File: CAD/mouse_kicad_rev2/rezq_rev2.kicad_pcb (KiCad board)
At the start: 2 copper layers, 92.8 x 89.3 mm, 99 parts, among them J2 SWD Header, M1 M1_Conn_Alt, M2 M2_Conn_Alt, Q0 TEFT4300, Q1 TEFT4300, Q10 Q_NMOS_GSD, Q11 Q_NMOS_GSD, Q12 Q_NMOS_GSD, Q2 TEFT4300, Q3 TEFT4300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

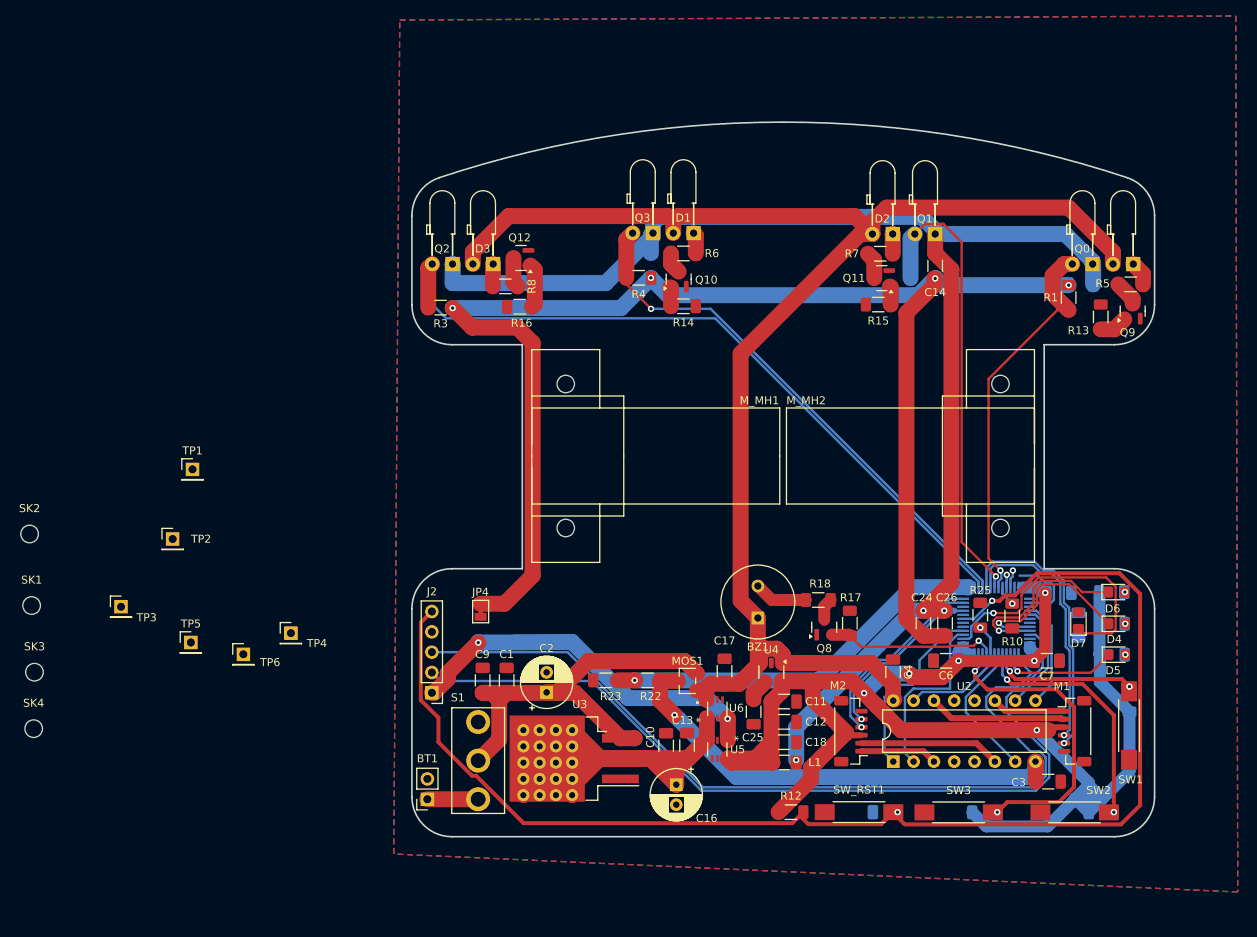
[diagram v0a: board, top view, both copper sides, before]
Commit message: Routed more of the schematic, connected all ground planes
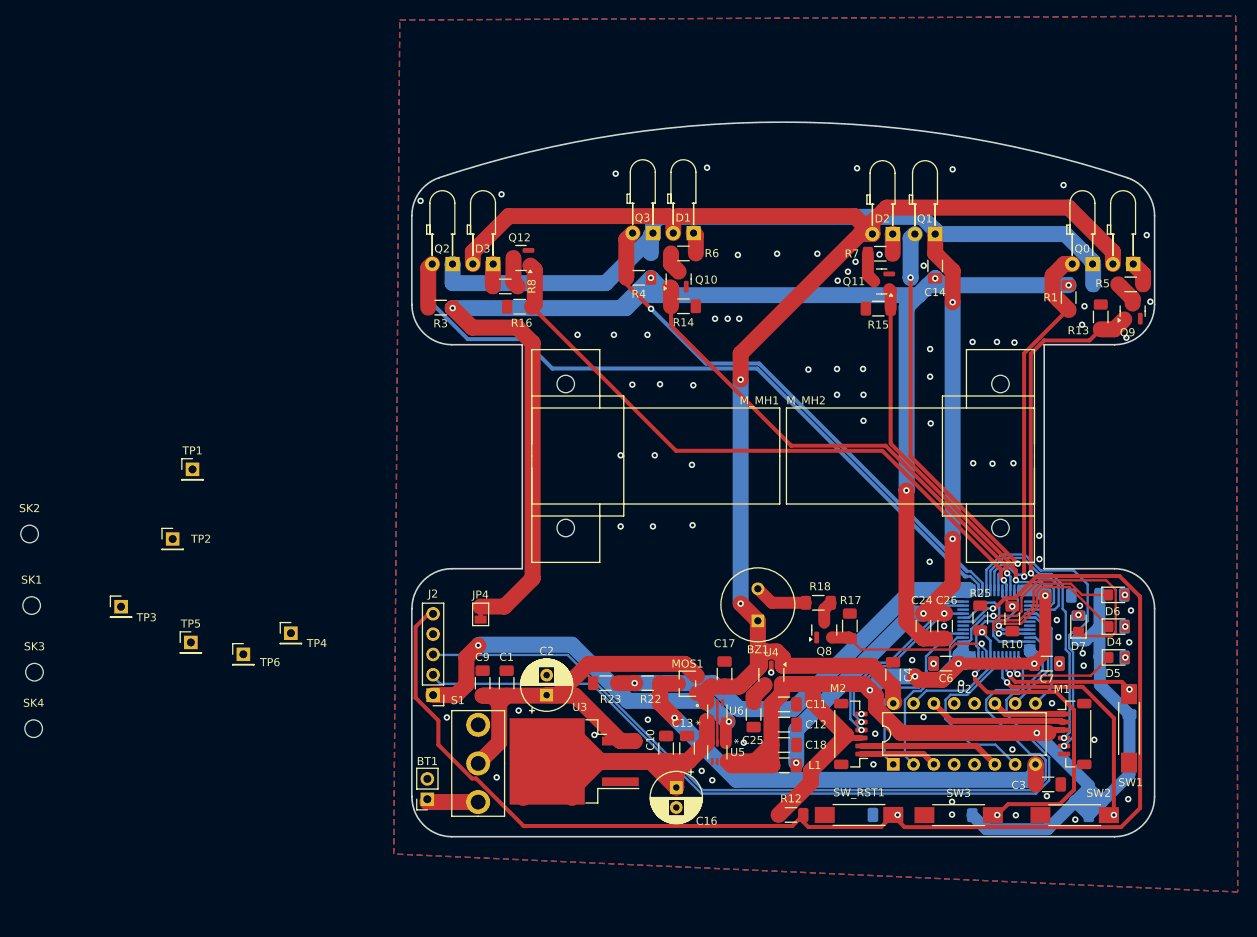
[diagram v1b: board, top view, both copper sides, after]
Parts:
- moved R15 0.51 mm to (211.5, 123.9)
- moved Q11 0.42 mm to (211.9, 120.5)
- moved C11 0.35 mm to (199.7, 173.3)
- moved C16 0.35 mm to (186.2, 183.7)
- moved C24 0.35 mm to (217.1, 163.6)
- moved C25 0.35 mm to (195.9, 174.6)
- moved C26 0.35 mm to (219.8, 163.6)
- moved D6 0.35 mm to (241.3, 159.7)
- moved M1 0.35 mm to (236.0, 177.1)
- moved M2 0.35 mm to (208.0, 177.1)
- moved Q8 0.35 mm to (204.7, 164.1)
- moved R21 0.35 mm to (240.6, 159.7)
- moved R25 0.35 mm to (224.2, 162.6)
- moved BZ1 0.35 mm to (196.4, 162.9)
- moved C1 0.35 mm to (165.0, 170.7)
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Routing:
- net EMIT_3: track 7.12 -> 80.6 mm
- net EMIT_2: track 4.65 -> 62.4 mm
- net EMIT_1: track 3.46 -> 51.3 mm, vias 0 -> 1
- net EMIT_4: track 12.1 -> 53.6 mm, vias 0 -> 1
- net Net-(U7-VSSA): track 0.00 -> 27.3 mm
- net AGND: track 179.2 -> 188.2 mm, vias 4 -> 5
- net RECEIV_2: track 58.1 -> 52.7 mm, vias 1 -> 2
- net M1_BACK: track 17.7 -> 22.8 mm
- net GND: track 0.00 -> 5.08 mm, vias 0 -> 87
- net M2_ENC_B: track 34.7 -> 39.7 mm
- net +3V3: track 194.6 -> 197.8 mm
- net V_METER: track 48.7 -> 51.4 mm
- net M1_FWD: track 22.4 -> 20.3 mm
- net RECEIV_1: track 48.7 -> 49.9 mm
- net +3V3_NET: track 46.9 -> 48.2 mm
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
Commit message: Prelim Final CAD
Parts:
- moved SK2 109.3 mm to (204.1, 105.3)
- moved SK1 106.4 mm to (196.2, 105.3)
- moved SK4 98.9 mm to (203.5, 192.1)
- moved SK3 92.5 mm to (195.6, 192.1)
- moved GND 88.2 mm to (211.4, 157.6)
- moved +5V 79.2 mm to (191.9, 186.4)
- moved GND 68.3 mm to (183.3, 129.1)
- moved +3v3V 61.7 mm to (195.7, 186.4)
- moved TP1 44.9 mm to (155.1, 177.8)
- moved GND 29.2 mm to (160.4, 160.1)
- moved JP4 2.55 mm to (164.3, 162.1)
- renumbered TP4 to +3v3V, TP3 to +5V, TP2 to GND, TP5 to GND, TP6 to GND
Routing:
- net Net-(S1-Pad3): track 0.00 -> 7.10 mm
- net +5V_NET: track 85.5 -> 92.3 mm
- net +3V3: track 197.8 -> 201.4 mm
- net AGND: track 188.2 -> 185.6 mm
- net RST: track 166.6 -> 167.5 mm
- net GND: vias 87 -> 88
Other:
- board size 92.8 x 89.3 mm -> 92.8 x 94.6 mm

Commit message: Final Layout
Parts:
- moved D1 5.77 mm to (187.8, 108.7), turned to -135 degrees
- moved D2 4.19 mm to (213.4, 110.4), turned to 135 degrees
- moved R7 3.10 mm to (211.6, 113.9)
- moved Q3 2.33 mm to (184.2, 112.3), turned to -135 degrees
- moved Q1 1.82 mm to (216.9, 113.9), turned to 135 degrees
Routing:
- net +3.3VA: track 175.8 -> 184.0 mm, vias 5 -> 6
- net AGND: track 185.6 -> 178.2 mm
- net +5V: track 192.5 -> 185.9 mm, vias 2 -> 3
- net Net-(D1-K): track 2.66 -> 8.64 mm
- net (no net): track 0.00 -> 3.43 mm
- net Net-(Q11-D): track 3.79 -> 6.95 mm
- net RECEIV_2: track 52.7 -> 55.4 mm
- net Net-(D2-K): track 2.47 -> 4.19 mm
- net RECEIV_3: track 67.6 -> 69.0 mm
- net GND: vias 88 -> 85
